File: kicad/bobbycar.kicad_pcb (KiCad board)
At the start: 2 copper layers, 42 x 45 mm, 66 parts, among them J10 BREMSE, J11 CAN2, J12 PROG, J13 LED, J2 IO2, J3 GAS, J4 TFT, J5 Conn_02x08_Odd_Even, J6 Conn_02x08_Odd_Even, J7 BREMSE, J8 GAS, Q1 SI2301CDS-T1-GE3, U1 ESP32-WROOM-32, U2 SN65HVD231, U3 USBLC6-4SC6, U4 USBLC6-4SC6, U5 MPM2359, U6 USBLC6-4SC6, U7 USBLC6-4SC6, U8 USBLC6-4SC6, U9 MCP1416

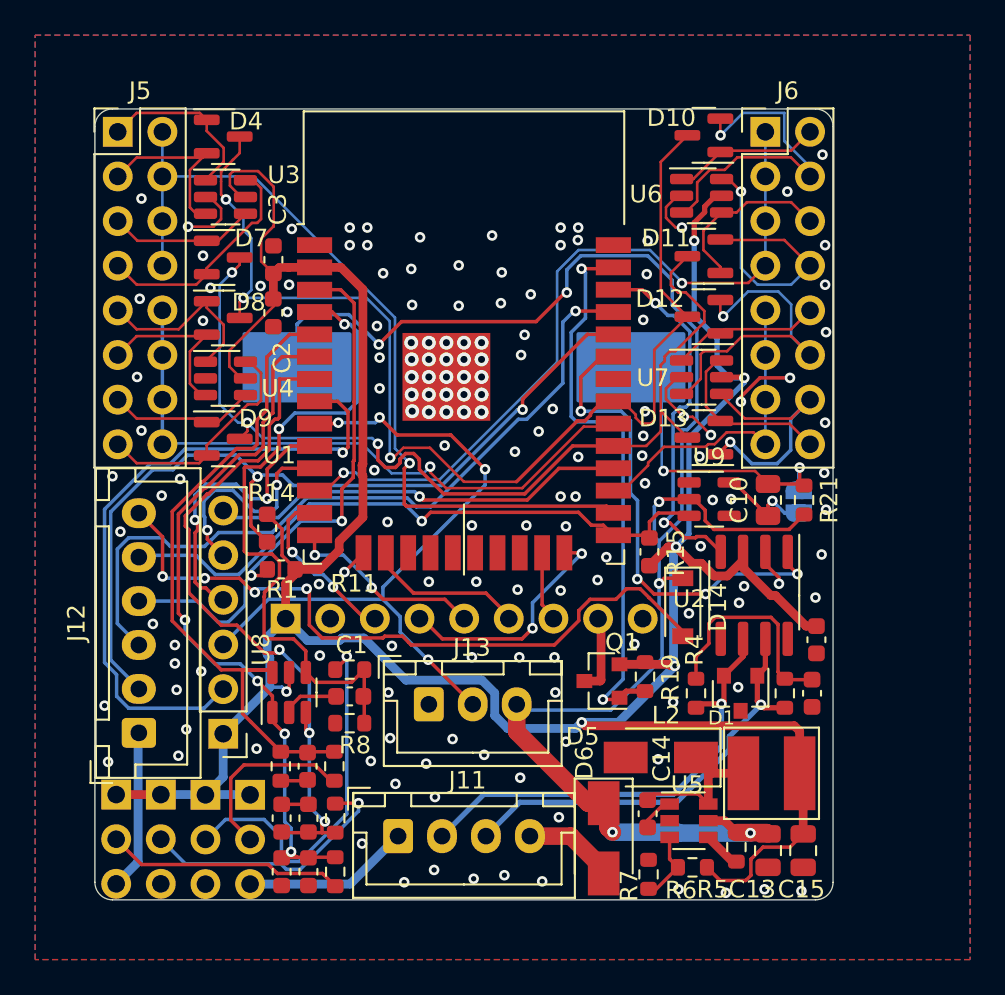
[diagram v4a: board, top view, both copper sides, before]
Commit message: Cleared pcb, added usb c
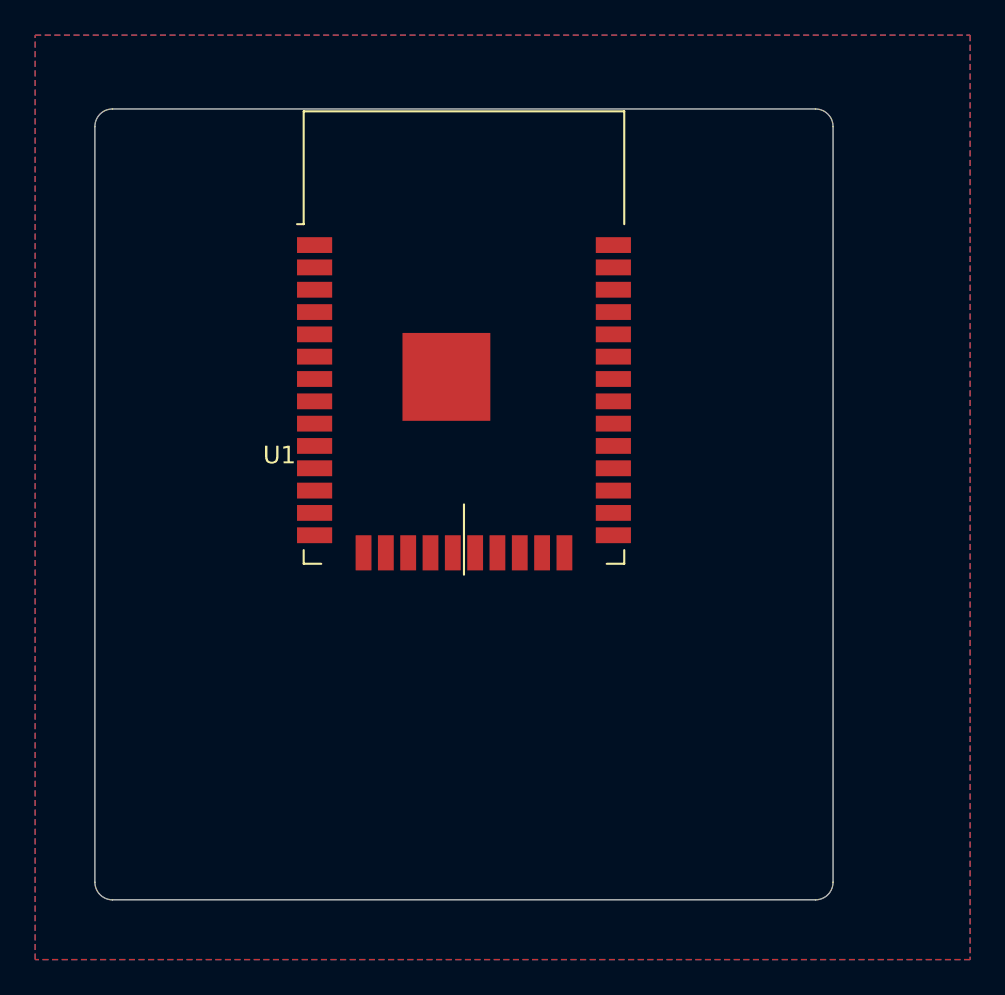
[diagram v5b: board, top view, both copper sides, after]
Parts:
- removed BZ1: Buzzer, Capacitor_SMD:CP_Elec_18x22
- removed C1, C3, C4, C5, C6, C7, C8: 100n, Capacitor_SMD:C_0603_1608Metric
- removed C10: 1u, Resistor_SMD:R_0805_2012Metric
- removed C13, C15: 22uF, Capacitor_SMD:C_0805_2012Metric
- removed C14: 10n, Capacitor_SMD:C_0603_1608Metric
- removed C2: 10u, Capacitor_SMD:C_0603_1608Metric
- removed D1: NUP2105L, Package_TO_SOT_SMD:SOT-23
- removed D10, D11, D12, D13, D4, D7, D8, D9: BAV99, Package_TO_SOT_SMD:SOT-23
- removed D14: D, Diode_SMD:D_SOD-123
- removed D5, D6: B230A, Diode_SMD:D_SMA
- removed J10, J7: BREMSE, Connector_PinHeader_2.54mm:PinHeader_1x03_P2.54mm_Vertical
- removed J11: CAN2, Connector_JST:JST_XH_B4B-XH-A_1x04_P2.50mm_Vertical
- removed J12: PROG, Connector_JST:JST_XH_B6B-XH-A_1x06_P2.50mm_Vertical
- removed J13: LED, Connector_JST:JST_XH_B3B-XH-A_1x03_P2.50mm_Vertical
- removed J2: IO2, Connector_PinHeader_2.54mm:PinHeader_1x06_P2.54mm_Vertical
- removed J3, J8: GAS, Connector_PinHeader_2.54mm:PinHeader_1x03_P2.54mm_Vertical
- removed J4: TFT, Connector_PinSocket_2.54mm:PinSocket_1x09_P2.54mm_Vertical
- removed J5, J6: Conn_02x08_Odd_Even, Connector_PinHeader_2.54mm:PinHeader_2x08_P2.54mm_Vertical
- removed JP1: Jumper_2_Open, Jumper:SolderJumper-2_P1.3mm_Open_RoundedPad1.0x1.5mm
- removed L2: 4.7uH, boardcomputer:L_5040
- removed Q1: SI2301CDS-T1-GE3, Package_TO_SOT_SMD:SOT-23
- removed R1, R14, R15, R5: 1k, Resistor_SMD:R_0603_1608Metric
- removed R10, R13, R16, R8: 100k, Resistor_SMD:R_0603_1608Metric
- removed R11, R12, R2, R9: 100r, Resistor_SMD:R_0603_1608Metric
- removed R19: 2k2, Resistor_SMD:R_0603_1608Metric
- removed R21: 4.7k, Resistor_SMD:R_0603_1608Metric
- removed R3, R4: 56R, Resistor_SMD:R_0603_1608Metric
- removed R6: 49.9k, Resistor_SMD:R_0603_1608Metric
- removed R7: 16.2k, Resistor_SMD:R_0603_1608Metric
- removed U2: SN65HVD231, Package_SO:SOIC-8_3.9x4.9mm_P1.27mm
- removed U3, U4, U6, U7, U8: USBLC6-4SC6, Package_TO_SOT_SMD:SOT-23-6
- removed U5: MPM2359, Package_TO_SOT_SMD:SOT-23-6
- removed U9: MCP1416, Package_TO_SOT_SMD:SOT-23-5
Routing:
- net +3V3: track 172.5 -> 0.00 mm, vias 6 -> 0
- net 15V: track 96.5 -> 0.00 mm, vias 6 -> 0
- net IO19: track 65.4 -> 0.00 mm, vias 3 -> 0
- net IO5: track 55.0 -> 0.00 mm, vias 3 -> 0
- net ESP_RX: track 49.6 -> 0.00 mm, vias 2 -> 0
- net IN1: track 47.4 -> 0.00 mm, vias 1 -> 0
- net GND: track 44.0 -> 0.00 mm, vias 155 -> 0
- net IN3: track 43.5 -> 0.00 mm, vias 2 -> 0
- net ESP_TX: track 42.7 -> 0.00 mm, vias 1 -> 0
- net RAW_GAS: track 40.1 -> 0.00 mm, vias 4 -> 0
- net Net-(D14-Pad2): track 39.7 -> 0.00 mm, vias 4 -> 0
- net RAW_BREMSE: track 39.7 -> 0.00 mm, vias 3 -> 0
- net IO33: track 39.2 -> 0.00 mm, vias 4 -> 0
- net RAW_M365_BREMS: track 38.2 -> 0.00 mm
- net RAW_M365_GAS: track 37.9 -> 0.00 mm, vias 2 -> 0
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
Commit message: Layout done
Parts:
- added C1: 100n, Capacitor_SMD:C_0603_1608Metric, F.Cu at (100.1, 61.1)
- added C13: 22uF, Capacitor_SMD:C_0805_2012Metric, F.Cu at (136.4, 49.9)
- added C14: 10n, Capacitor_SMD:C_0603_1608Metric, F.Cu at (133.8, 50.7)
- added C15: 22uF, Capacitor_SMD:C_0805_2012Metric, F.Cu at (128.1, 56.5)
- added C2: 10u, Capacitor_SMD:C_0603_1608Metric, F.Cu at (103.4, 35.4)
- added C3: 100n, Capacitor_SMD:C_0603_1608Metric, F.Cu at (105.6, 34.5)
- added C4: 100n, Capacitor_SMD:C_0603_1608Metric, F.Cu at (104.3, 63.8)
- added C5: 100n, Capacitor_SMD:C_0603_1608Metric, F.Cu at (110.4, 66.6)
- added C6: 100n, Capacitor_SMD:C_0603_1608Metric, F.Cu at (100.1, 64.0)
- added C7: 100n, Capacitor_SMD:C_0603_1608Metric, F.Cu at (98.5, 64.0)
- added C8: 100n, Capacitor_SMD:C_0603_1608Metric, F.Cu at (98.5, 61.1)
- added C9: 100n, Capacitor_SMD:C_0603_1608Metric, F.Cu at (126.0, 60.5)
- added D1: NUP2105L, Package_TO_SOT_SMD:SOT-23, F.Cu at (107.1, 71.1)
- added D10: BAV99, Package_TO_SOT_SMD:SOT-23, F.Cu at (101.7, 31.0)
- added D11: BAV99, Package_TO_SOT_SMD:SOT-23, F.Cu at (101.7, 34.3)
- added D12: BAV99, Package_TO_SOT_SMD:SOT-23, F.Cu at (102.0, 40.9)
- added D13: BAV99, Package_TO_SOT_SMD:SOT-23, F.Cu at (102.1, 44.2)
- added D2: D, Diode_SMD:D_SOD-123, F.Cu at (121.1, 66.2)
- added D4: BAV99, Package_TO_SOT_SMD:SOT-23, F.Cu at (129.6, 29.8)
- added D5: B230A, Diode_SMD:D_SMA, F.Cu at (135.6, 55.2)
- added D6: B230A, Diode_SMD:D_SMA, F.Cu at (115.4, 66.2)
- added D7: BAV99, Package_TO_SOT_SMD:SOT-23, F.Cu at (129.6, 33.3)
- added D8: BAV99, Package_TO_SOT_SMD:SOT-23, F.Cu at (129.6, 40.3)
- added D9: BAV99, Package_TO_SOT_SMD:SOT-23, F.Cu at (129.6, 43.7)
- added J10: BREMSE, Connector_PinHeader_2.54mm:PinHeader_1x03_P2.54mm_Vertical, F.Cu at (103.0, 66.7)
- added J11: CAN2, Connector_JST:JST_XH_B4B-XH-A_1x04_P2.50mm_Vertical, F.Cu at (119.8, 71.3)
- added J13: LED, Connector_JST:JST_XH_B3B-XH-A_1x03_P2.50mm_Vertical, F.Cu at (118.6, 61.9)
- added J2: IO2, boardcomputer:PinHeader_2x04_P2.54mm_Vertical_7Pin, F.Cu at (96.3, 49.3)
- added J3: GAS, Connector_PinHeader_2.54mm:PinHeader_1x03_P2.54mm_Vertical, F.Cu at (96.2, 66.7)
- added J4: TFT, Connector_PinSocket_2.54mm:PinSocket_1x09_P2.54mm_Vertical, F.Cu at (126.2, 56.6)
- added J5: Conn_02x08_Odd_Even, Connector_PinHeader_2.54mm:PinHeader_2x08_P2.54mm_Vertical, F.Cu at (133.3, 29.1)
- added J6: Conn_02x08_Odd_Even, Connector_PinHeader_2.54mm:PinHeader_2x08_P2.54mm_Vertical, F.Cu at (96.3, 29.1)
- added J7: BREMSE, Connector_PinHeader_2.54mm:PinHeader_1x03_P2.54mm_Vertical, F.Cu at (98.5, 66.7)
- added J8: GAS, Connector_PinHeader_2.54mm:PinHeader_1x03_P2.54mm_Vertical, F.Cu at (100.8, 66.7)
- added JP2: SolderJumper_2_Open, Jumper:SolderJumper-2_P1.3mm_Open_RoundedPad1.0x1.5mm, B.Cu at (110.6, 53.7)
- added JP3: SolderJumper_2_Open, Jumper:SolderJumper-2_P1.3mm_Open_RoundedPad1.0x1.5mm, B.Cu at (108.3, 53.7)
- added JP4: SolderJumper_2_Open, Jumper:SolderJumper-2_P1.3mm_Open_RoundedPad1.0x1.5mm, B.Cu at (106.0, 53.7)
- added JP5: SolderJumper_2_Open, Jumper:SolderJumper-2_P1.3mm_Open_RoundedPad1.0x1.5mm, B.Cu at (103.7, 53.7)
- added L2: 4.7uH, boardcomputer:L_5040, F.Cu at (131.6, 55.7)
- added Q1: SI2301CDS-T1-GE3, Package_TO_SOT_SMD:SOT-23, F.Cu at (103.5, 50.7)
- added Q2: SS8050_C2150, Package_TO_SOT_SMD:TSOT-23, F.Cu at (124.9, 68.9)
- added Q3: SS8050_C2150, Package_TO_SOT_SMD:TSOT-23, F.Cu at (124.9, 64.5)
- added R1: 10k, Resistor_SMD:R_0603_1608Metric, F.Cu at (105.6, 37.5)
- added R10: 100k, Resistor_SMD:R_0603_1608Metric, F.Cu at (102.8, 61.2)
- added R11: 100r, Resistor_SMD:R_0603_1608Metric, F.Cu at (101.4, 64.0)
- added R12: 100r, Resistor_SMD:R_0603_1608Metric, F.Cu at (102.8, 64.0)
- added R13: 100k, Resistor_SMD:R_0603_1608Metric, F.Cu at (95.7, 61.2)
- added R14: 1k, Resistor_SMD:R_0603_1608Metric, F.Cu at (126.7, 41.8)
- added R15: 10k, Resistor_SMD:R_0603_1608Metric, F.Cu at (126.6, 53.3)
- added R16: 100k, Resistor_SMD:R_0603_1608Metric, F.Cu at (97.1, 61.2)
- added R17: 5k1, Resistor_SMD:R_0603_1608Metric, F.Cu at (123.5, 71.5)
- added R18: 5k1, Resistor_SMD:R_0603_1608Metric, F.Cu at (126.2, 71.5)
- added R19: 2k2, Resistor_SMD:R_0603_1608Metric, F.Cu at (100.7, 51.0)
- added R2: 100r, Resistor_SMD:R_0603_1608Metric, F.Cu at (95.7, 64.0)
- added R20: 12k, Resistor_SMD:R_0603_1608Metric, F.Cu at (123.7, 61.1)
- added R22: 12k, Resistor_SMD:R_0603_1608Metric, F.Cu at (122.5, 63.5)
- added R3: 56R, Resistor_SMD:R_0603_1608Metric, F.Cu at (108.1, 67.5)
- added R4: 56R, Resistor_SMD:R_0603_1608Metric, F.Cu at (106.0, 67.5)
- added R5: 1k, Resistor_SMD:R_0603_1608Metric, F.Cu at (133.9, 48.7)
- added R6: 49.9k, Resistor_SMD:R_0603_1608Metric, F.Cu at (128.0, 53.3)
- added R7: 16.2k, Resistor_SMD:R_0603_1608Metric, F.Cu at (130.3, 52.3)
- added R8: 100k, Resistor_SMD:R_0603_1608Metric, F.Cu at (101.4, 61.2)
- added R9: 100r, Resistor_SMD:R_0603_1608Metric, F.Cu at (97.1, 64.0)
- added U10: CH343G, Package_SO:SOIC-16_3.9x9.9mm_P1.27mm, F.Cu at (131.9, 62.5)
- added U2: SN65HVD231, Package_SO:SOIC-8_3.9x4.9mm_P1.27mm, F.Cu at (107.8, 62.2)
- added U3: USBLC6-4SC6, Package_TO_SOT_SMD:SOT-23-6, F.Cu at (129.5, 36.8)
- added U4: USBLC6-4SC6, Package_TO_SOT_SMD:SOT-23-6, F.Cu at (129.5, 47.1)
- added U5: MPM2359, Package_TO_SOT_SMD:SOT-23-6, F.Cu at (127.9, 50.2)
- added U6: USBLC6-4SC6, Package_TO_SOT_SMD:SOT-23-6, F.Cu at (102.2, 37.5)
- added U7: USBLC6-4SC6, Package_TO_SOT_SMD:SOT-23-6, F.Cu at (102.2, 47.6)
- added U8: USBLC6-4SC6, Package_TO_SOT_SMD:SOT-23-6, F.Cu at (100.1, 57.7)
- added USBC1: MC-311D, usb_c_bobby:USB-C-SMD_MC-311D, F.Cu at (131.8, 69.3)
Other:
- board text added: "+15V"
- board text added: "+3V3"
- board text added: "BLACK Display"
- board text added: "BREMS"
- board text added: "CANH"
- board text added: "CANL"
- board text added: "GAS"
- board text added: "M365"
- board text added: "RED Display"
- board text added: "STD"
- board text removed: "15V D+ D- GND"
- board text removed: "15V LED GND"
- board text removed: "3V3"
- board text removed: "3v3 3V3 3V3 3V3 BRE3 GAS3 BRE GAS GND GND GND GND"
- board text removed: "Analog"
- board text removed: "CAN"
- board text removed: "CS"
- board text removed: "DC"
- board text removed: "DC speaker"
- board text removed: "Flash"
- board text removed: "GPIO"
- board text removed: "IO17 IO26 IO25 IO33 IO32 3V3"
- board text removed: "IO33"
- board text removed: "RES"
- board text removed: "SCK"
- board text removed: "SDI"
- board text removed: "SDO"
- board text removed: "TFT"
- board text removed: "VIN IO0 EN TX RX GND"

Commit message: Half done trace layout
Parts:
- moved JP5 2.02 mm to (105.7, 54.0)
- moved JP4 1.62 mm to (107.6, 54.0)
- moved JP3 1.23 mm to (109.5, 54.0)
- moved JP2 0.84 mm to (111.4, 54.0)
- moved C13 0.18 mm to (136.2, 49.9)
- moved U10 0.15 mm to (131.9, 62.4)
- moved U5 0.05 mm to (127.9, 50.1)
- turned U8 to 0 degrees
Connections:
- Q1 pad 1: Net-(Q1-Pad1) -> TFT_LED
- R19 pad 1: Net-(Q1-Pad1) -> TFT_LED
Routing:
- net +3V3: track 0.00 -> 119.0 mm, vias 0 -> 10
- net IO5: track 0.00 -> 70.3 mm, vias 0 -> 7
- net IO19: track 0.00 -> 38.4 mm, vias 0 -> 3
- net IO17: track 0.00 -> 37.9 mm, vias 0 -> 2
- net IN4: track 0.00 -> 37.4 mm, vias 0 -> 1
- net CAN_RX: track 0.00 -> 36.8 mm, vias 0 -> 2
- net TFT_LED: track 0.00 -> 36.6 mm, vias 0 -> 2
- net RAW_M365_BREMS: track 0.00 -> 35.4 mm, vias 0 -> 2
- net ESP_RX: track 0.00 -> 35.0 mm, vias 0 -> 2
- net ESP_TX: track 0.00 -> 34.3 mm, vias 0 -> 2
- net RAW_M365_GAS: track 0.00 -> 33.9 mm, vias 0 -> 4
- net +5V: track 0.00 -> 32.4 mm, vias 0 -> 4
- net RAW_GAS: track 0.00 -> 31.9 mm
- net IN1: track 0.00 -> 31.8 mm, vias 0 -> 1
- net CAN_TX: track 0.00 -> 30.3 mm, vias 0 -> 2
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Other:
- board text added: "(MISO)"
- board text added: "CLK"
- board text added: "CS"
- board text added: "DC"
- board text added: "MOSI"
- board text added: "RST"
